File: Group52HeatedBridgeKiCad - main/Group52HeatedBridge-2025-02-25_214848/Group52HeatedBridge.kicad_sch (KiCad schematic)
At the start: 21 parts

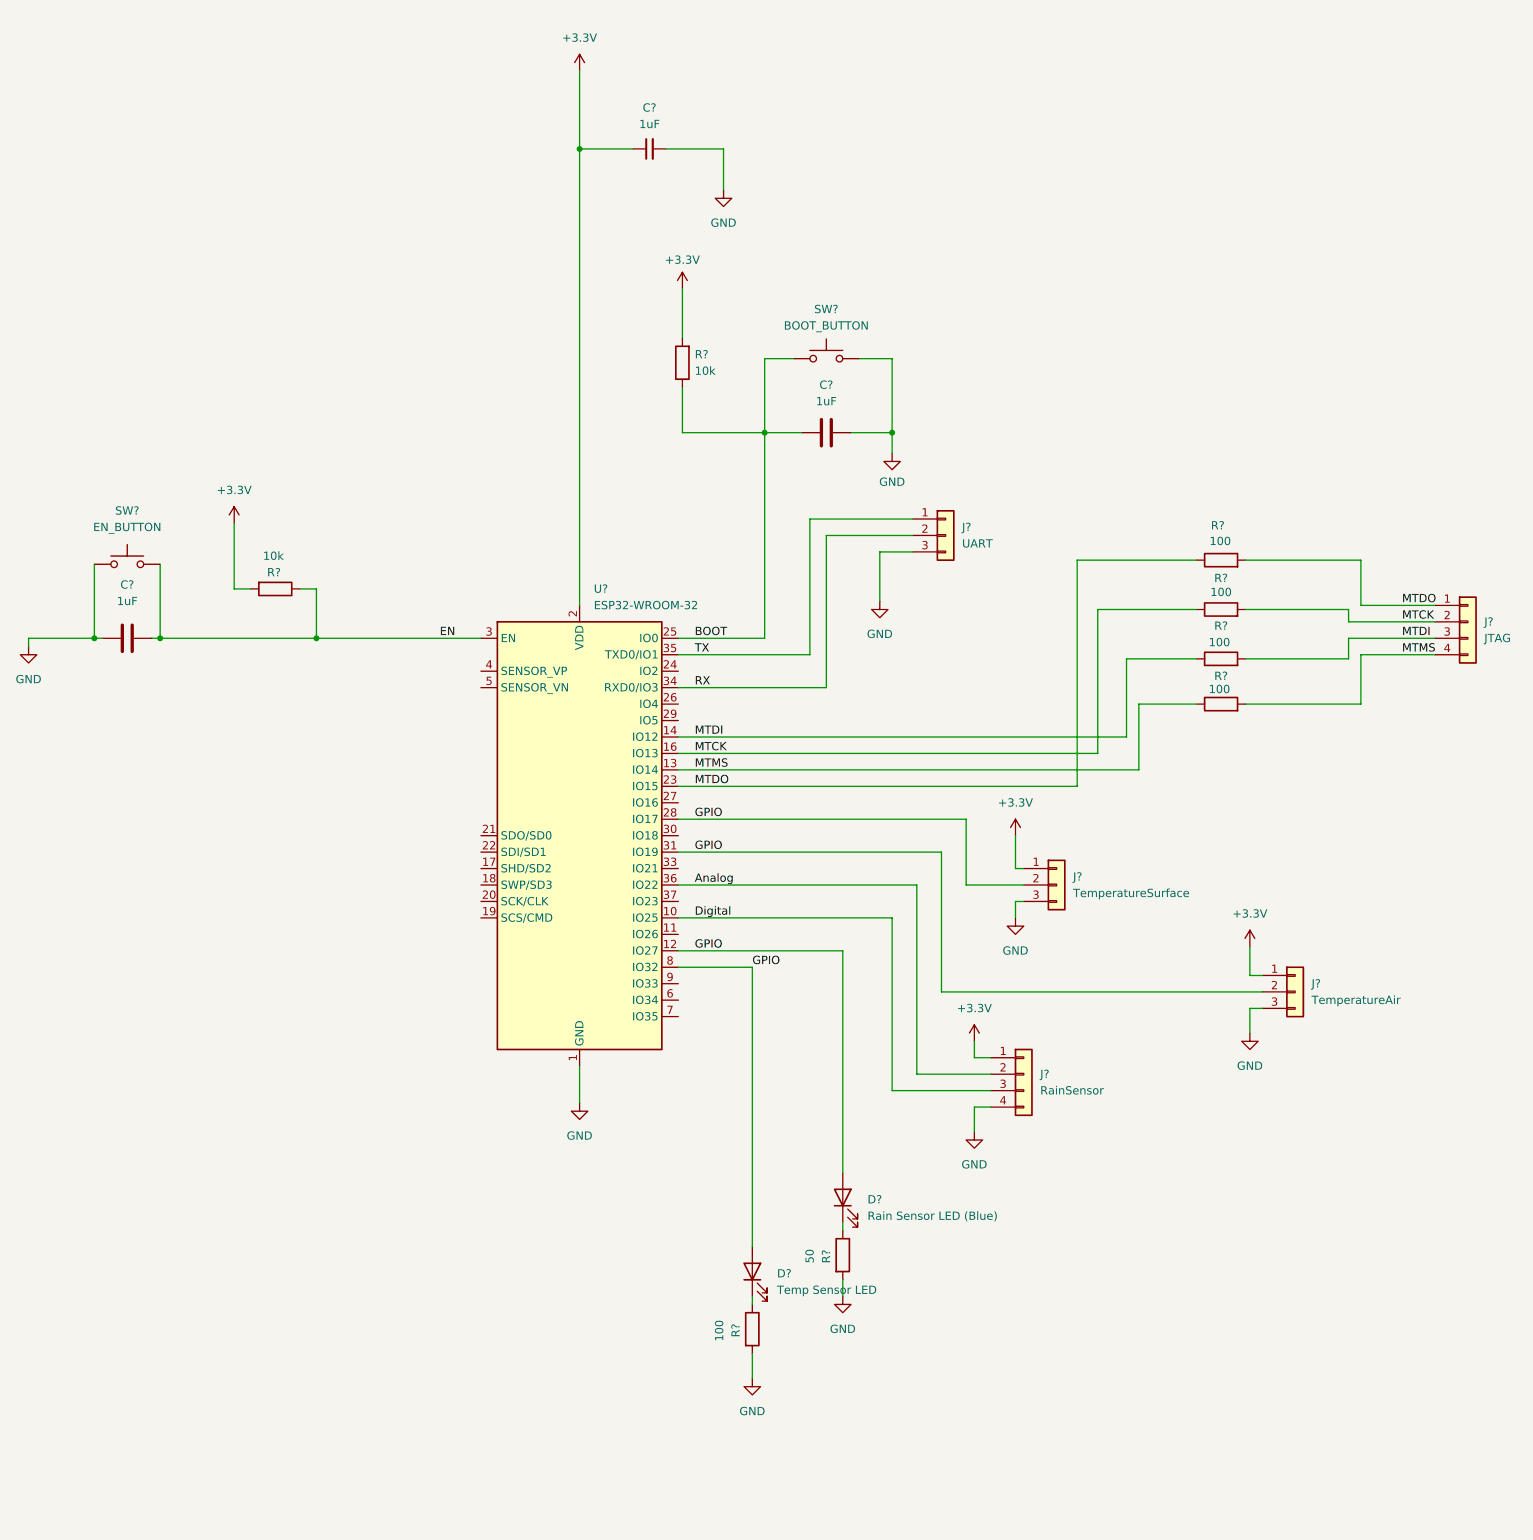
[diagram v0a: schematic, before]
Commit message: scematic passes DRC except one error where we need to draw the actual physical border of our PCB, components are flipped tho
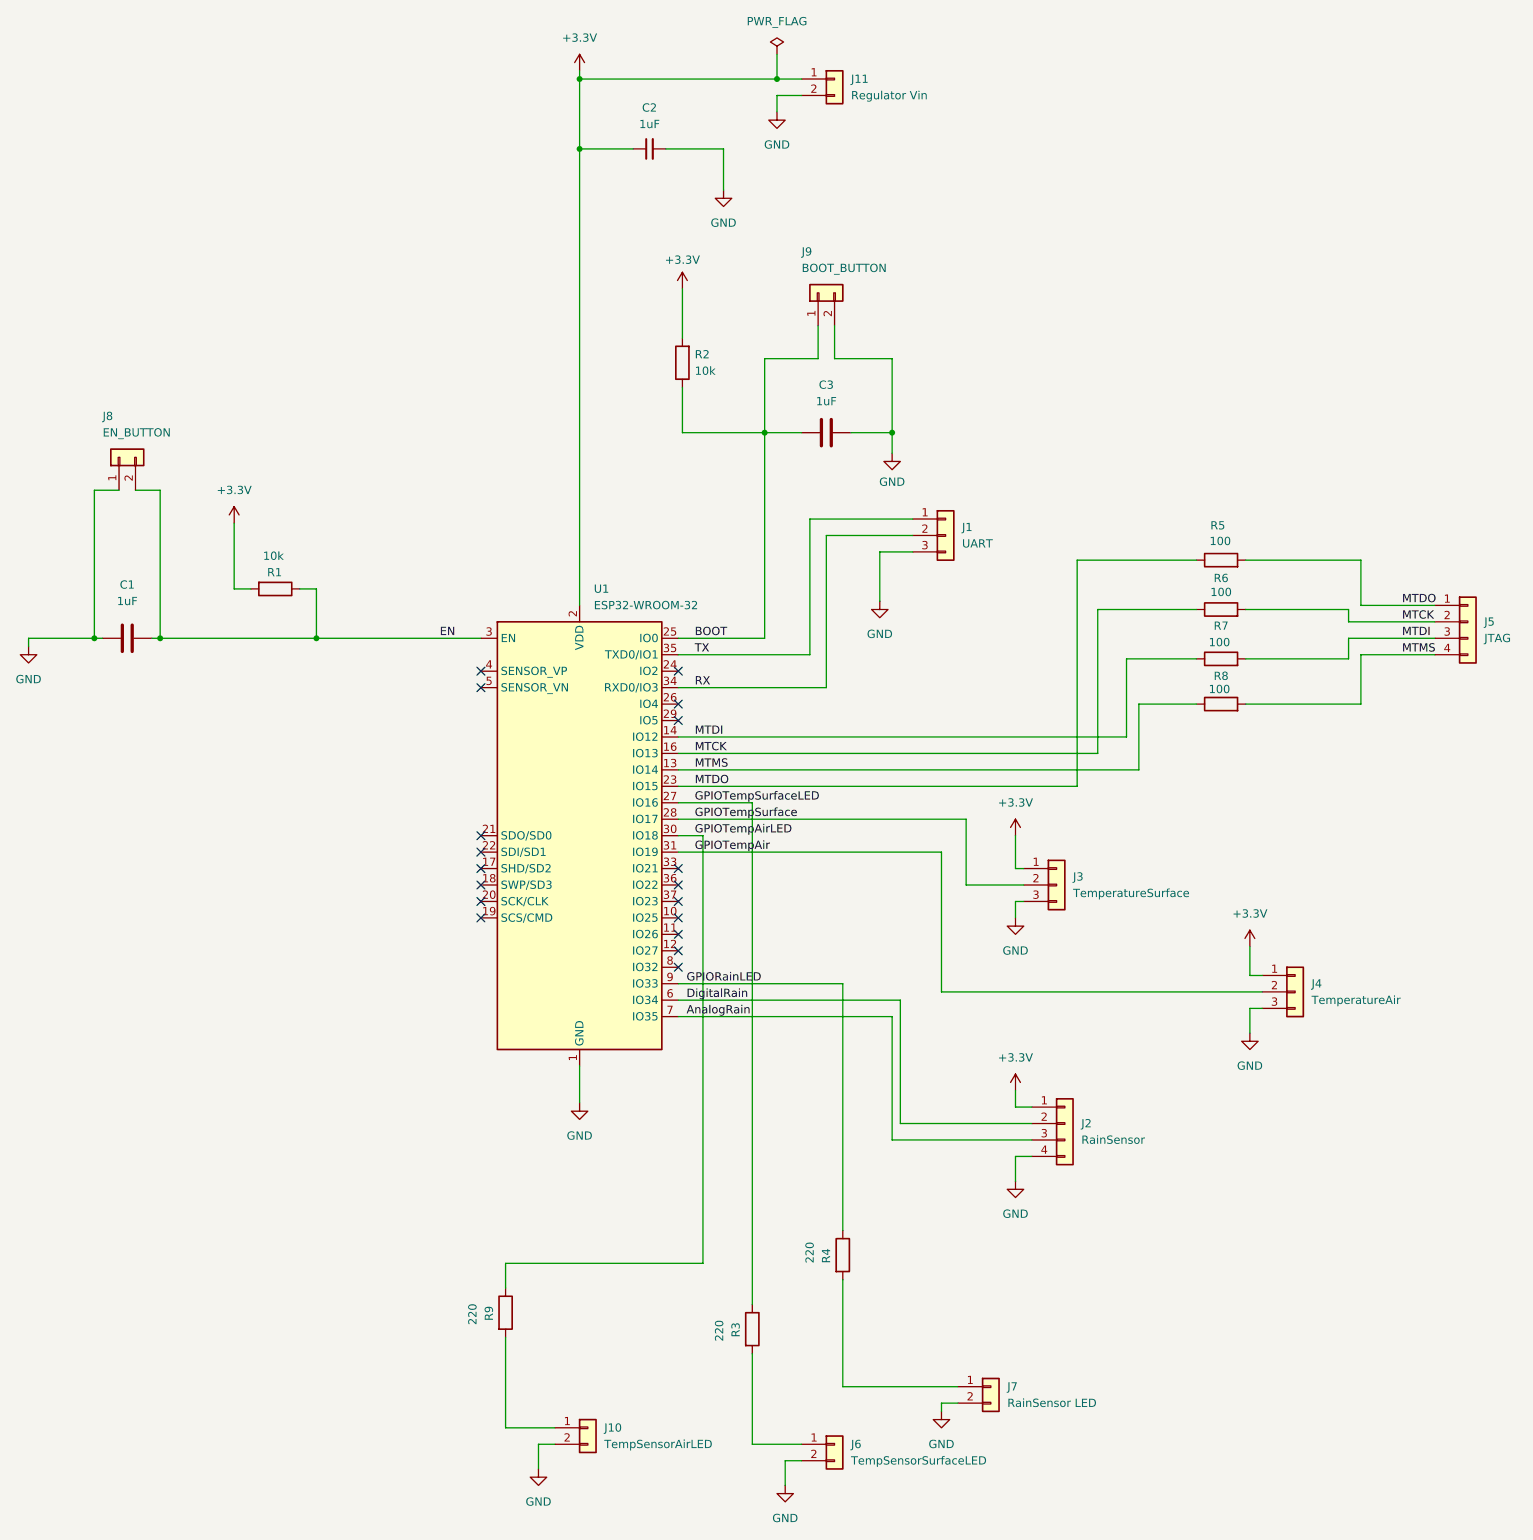
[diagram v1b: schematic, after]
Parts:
- removed D?: Temp Sensor LED, symbol Device:LED
- removed D?: Rain Sensor LED (Blue), symbol Device:LED
- removed SW?: BOOT_BUTTON, symbol Switch:SW_Push
- removed SW?: EN_BUTTON, symbol Switch:SW_Push
- added J10: TempSensorAirLED, Connector_Molex:Molex_KK-254_AE-6410-02A_1x02_P2.54mm_Vertical, symbol Connector_Generic:Conn_01x02
- added J11: Regulator Vin, Connector_Molex:Molex_KK-254_AE-6410-02A_1x02_P2.54mm_Vertical, symbol Connector_Generic:Conn_01x02
- added J6: TempSensorSurfaceLED, Connector_Molex:Molex_KK-254_AE-6410-02A_1x02_P2.54mm_Vertical, symbol Connector_Generic:Conn_01x02
- added J7: RainSensor LED, Connector_Molex:Molex_KK-254_AE-6410-02A_1x02_P2.54mm_Vertical, symbol Connector_Generic:Conn_01x02
- added J8: EN_BUTTON, Connector_Molex:Molex_KK-254_AE-6410-02A_1x02_P2.54mm_Vertical, symbol Connector_Generic:Conn_01x02
- added J9: BOOT_BUTTON, Connector_Molex:Molex_KK-254_AE-6410-02A_1x02_P2.54mm_Vertical, symbol Connector_Generic:Conn_01x02
- added R9: 220, Resistor_SMD:R_0805_2012Metric_Pad1.20x1.40mm_HandSolder, symbol Device:R
- C1, C2, C3: renamed from C?; footprint (none) -> Capacitor_SMD:C_0805_2012Metric_Pad1.18x1.45mm_HandSolder
- J1, J3, J4: renamed from J?; footprint (none) -> Connector_Molex:Molex_KK-254_AE-6410-03A_1x03_P2.54mm_Vertical
- J2, J5: renamed from J?; footprint (none) -> Connector_Molex:Molex_KK-254_AE-6410-04A_1x04_P2.54mm_Vertical
- R1, R2, R5, R6, R7, R8: renamed from R?; footprint (none) -> Resistor_SMD:R_0805_2012Metric_Pad1.20x1.40mm_HandSolder
- R3: renamed from R?; value 100 -> 220; footprint (none) -> Resistor_SMD:R_0805_2012Metric_Pad1.20x1.40mm_HandSolder
- R4: renamed from R?; value 50 -> 220; footprint (none) -> Resistor_SMD:R_0805_2012Metric_Pad1.20x1.40mm_HandSolder
- gave numbers to parts that had none: 1
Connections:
- net +3.3V: now also J11.1 (Pin_1)
- net BOOT: now also J9.1 (Pin_1)
- net EN: now also J8.2 (Pin_2)
- net GND: now also J10.2 (Pin_2), J11.2 (Pin_2), J6.2 (Pin_2), J7.2 (Pin_2), J8.1 (Pin_1), J9.2 (Pin_2); no longer R3.2, R4.2
- net GPIOTempSurfaceLED: now reaches R3.1
- net GPIOTempSurfaceLED: now also U1.27 (IO16)
- net GPIOTempAirLED: now reaches U1.30 (IO18)
- net GPIOTempAirLED: now also R9.1
- net DigitalRain: now reaches U1.6 (IO34)
- net DigitalRain: now also J2.2 (Pin_2)
- net AnalogRain: now reaches U1.7 (IO35)
- net AnalogRain: now also J2.3 (Pin_3)
- net GPIORainLED: now reaches U1.9 (IO33)
- net GPIORainLED: now also R4.1
- net Analog: no longer names the net of U1.36 (IO22)
- net Analog: no longer J2.2 (Pin_2)
- net Digital: no longer names the net of U1.10 (IO25)
- net Digital: no longer J2.3 (Pin_3)
- removed net GPIO: J3.2 (Pin_2), J4.2 (Pin_2), U1.12 (IO27), U1.28 (IO17), U1.31 (IO19), U1.8 (IO32)
- new net: J10.1 (Pin_1), R9.2
- new net: J7.1 (Pin_1), R4.2
- new net: J6.1 (Pin_1), R3.2
- new net GPIOTempAir: J4.2 (Pin_2), U1.31 (IO19)
- new net GPIOTempSurface: J3.2 (Pin_2), U1.28 (IO17)
- no-connect marks 0 -> 18
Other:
- moved on the sheet: J2
